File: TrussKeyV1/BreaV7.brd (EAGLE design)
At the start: 39.6 x 19 mm, 46 parts, among them J2 XF2L-0535-1, Q1 ABM-16MHZ, SW1 LS12T2-T, SW2 EVQ11U09K, SW3 ESE31L11T, U2 TPS62200, U5 MCP73831T-2ACI/OT, U6 MAX17044, X1 CON-1PIN, X3 CON-1PIN, X4 MicroB

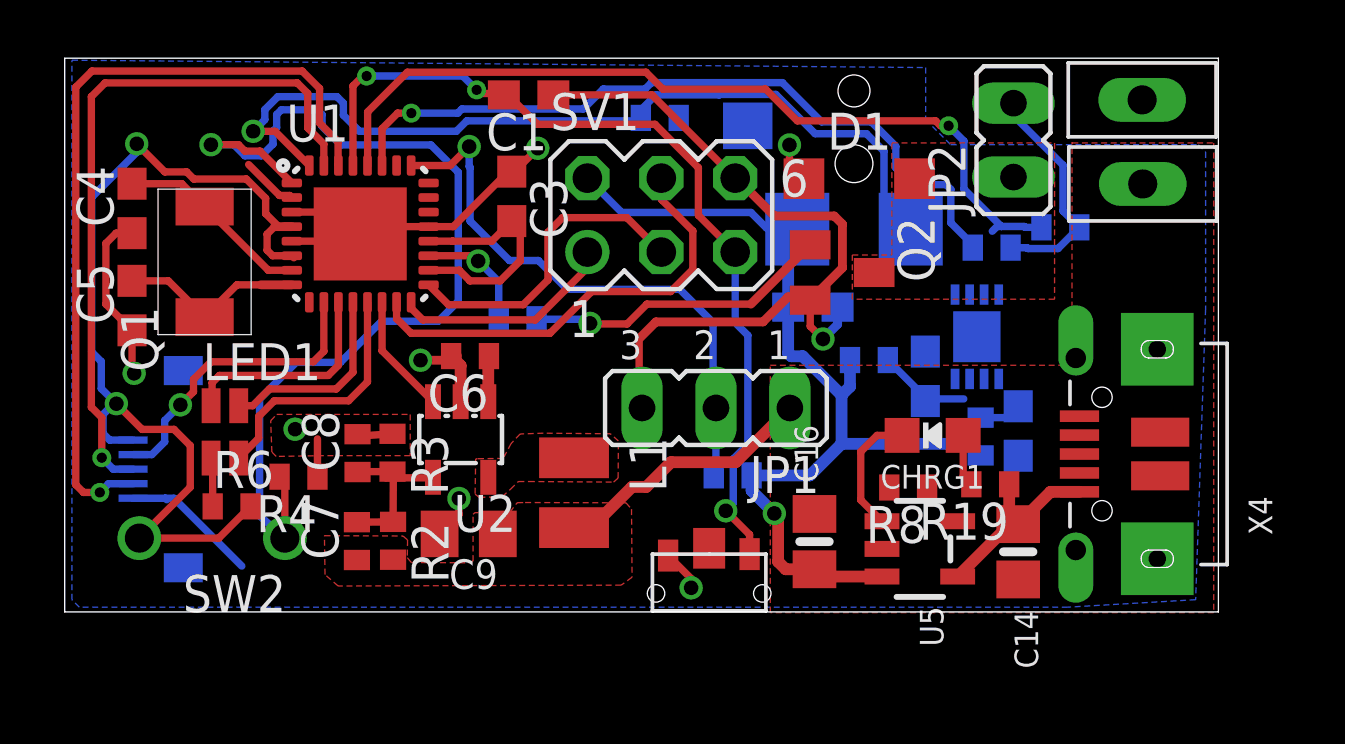
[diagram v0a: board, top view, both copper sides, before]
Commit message: Layout change
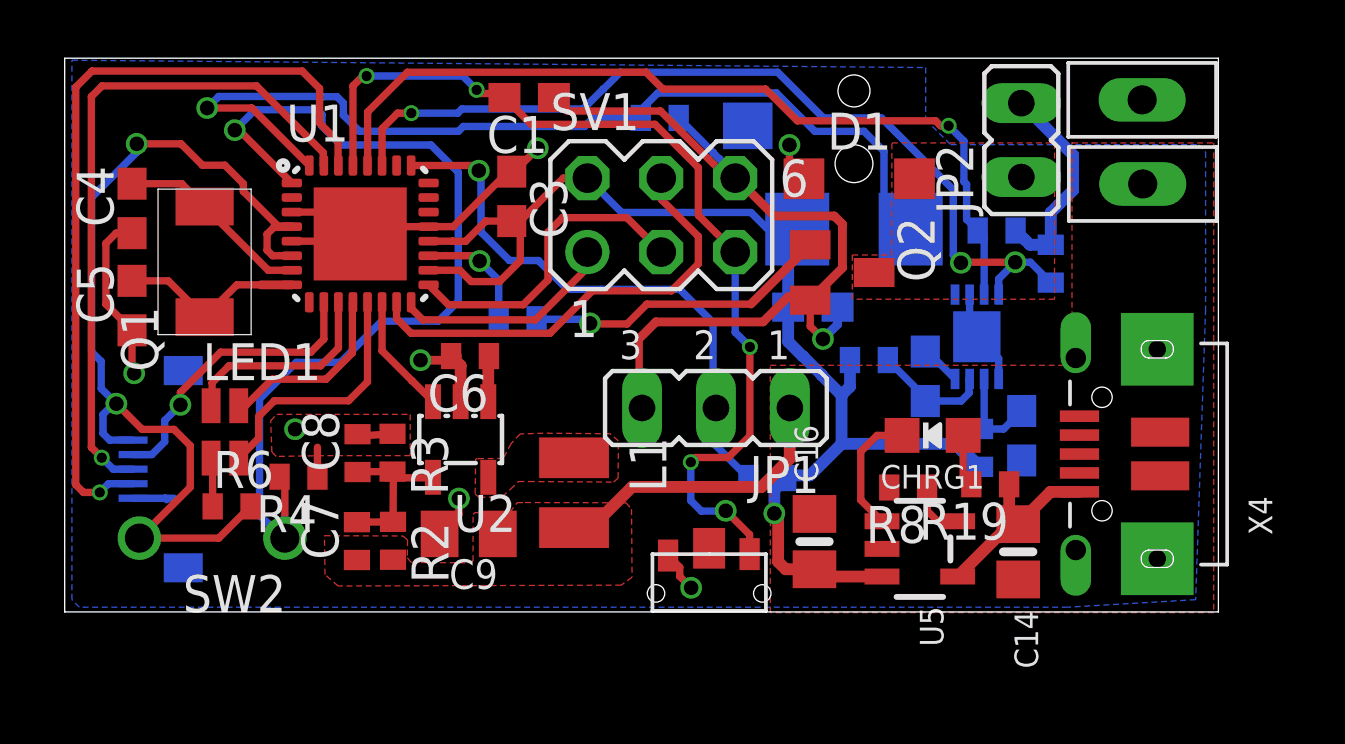
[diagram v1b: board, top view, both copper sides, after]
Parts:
- moved R16 2.19 mm to (32.0, 13.1)
- moved R15 2.10 mm to (33.9, 11.9), turned to 90 degrees
- moved R1 1.19 mm to (24.1, 4.57)
- moved R17 0.39 mm to (31.5, 5.60)
- moved JP2 0.27 mm to (32.9, 16.2)
- moved C17 0.20 mm to (32.9, 6.02)
- moved C1 0.09 mm to (16.0, 17.6)
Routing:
- net SDA: track 25.7 -> 30.7 mm, vias 1 -> 3
- net DETSW: track 30.5 -> 33.6 mm
- net GND: track 59.4 -> 62.3 mm
- net PWRSW: track 34.3 -> 31.8 mm
- net RST: track 30.7 -> 33.0 mm, vias 3 -> 5
- net N$13: track 1.45 -> 3.46 mm
- net N$12: track 0.00 -> 2.00 mm
- net LEDSOC: track 1.96 -> 0.00 mm
- net TX: track 24.3 -> 23.3 mm
- net N$15: track 3.49 -> 4.15 mm
- net VCC: track 84.8 -> 85.3 mm

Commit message: DRC approved
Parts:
- moved R18 0.42 mm to (27.8, 8.25), turned to 270 degrees
- moved R19 0.32 mm to (32.0, 4.57)
- moved R15 0.24 mm to (34.1, 12.1)
- moved C17 0.15 mm to (33.0, 6.02)
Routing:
- net GND: track 62.3 -> 61.3 mm
- net VOUT: track 9.57 -> 10.1 mm

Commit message: V7 Gerber final
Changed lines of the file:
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@@
 <contactref element="U6" pad="3"/>
 <wire x1="29.750096875" y1="7.212075" x2="29.58" y2="7.21" width="0.254" layer="16"/>
-<wire x1="29.625" y1="7.285" x2="29.697925" y2="7.212075" width="0.254" layer="16"/>
 <wire x1="29.697925" y1="7.212075" x2="29.750096875" y2="7.212075" width="0.254" layer="16"/>
 <wire x1="30.80905" y1="7.212075" x2="29.750096875" y2="7.212075" width="0.254" layer="16"/>

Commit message: Fusion PCBA
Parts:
- removed C15: 10nF, rcl:C0603
- removed R17: 1K, resistor:R0402
- removed R18: 180, resistor:R0402
- removed U6: MAX17044, NewPart:TDFN
- added U3: LC709203, NewPart:WDFN8
- R15, R16: value 4.7K -> 10K
- R7: value 330 -> 1K
- moved R15 1.42 mm to (33.4, 10.8), turned to 180 degrees
- moved R16 0.54 mm to (32.5, 13.2)
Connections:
- removed net N$13: C17.1, R17.2, U6.2
- removed net N$15: C15.1, R18.2, U6.3
- new net VBAT: C17.2, U3.3
- net GND: now also C17.1, U3.1, U3.2, U3.9; no longer C15.2, C17.2, U6.1, U6.4, U6.6, U6.9
- net SCL: now also R15.1, U3.8; no longer R16.1, U6.7
- net SDA: now also R16.1, U3.7; no longer R15.1, U6.8
- net VCC: no longer R17.1, R18.1
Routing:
- net N$15: track 4.06 -> 0.00 mm
- net VBAT: track 0.00 -> 4.05 mm
- net N$13: track 3.61 -> 0.00 mm
- net GND: track 61.3 -> 59.1 mm
- net SCL: track 29.4 -> 30.7 mm
- net SDA: track 30.9 -> 30.3 mm
